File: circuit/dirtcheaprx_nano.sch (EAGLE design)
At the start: 20 parts, among them IC1 MCP1700

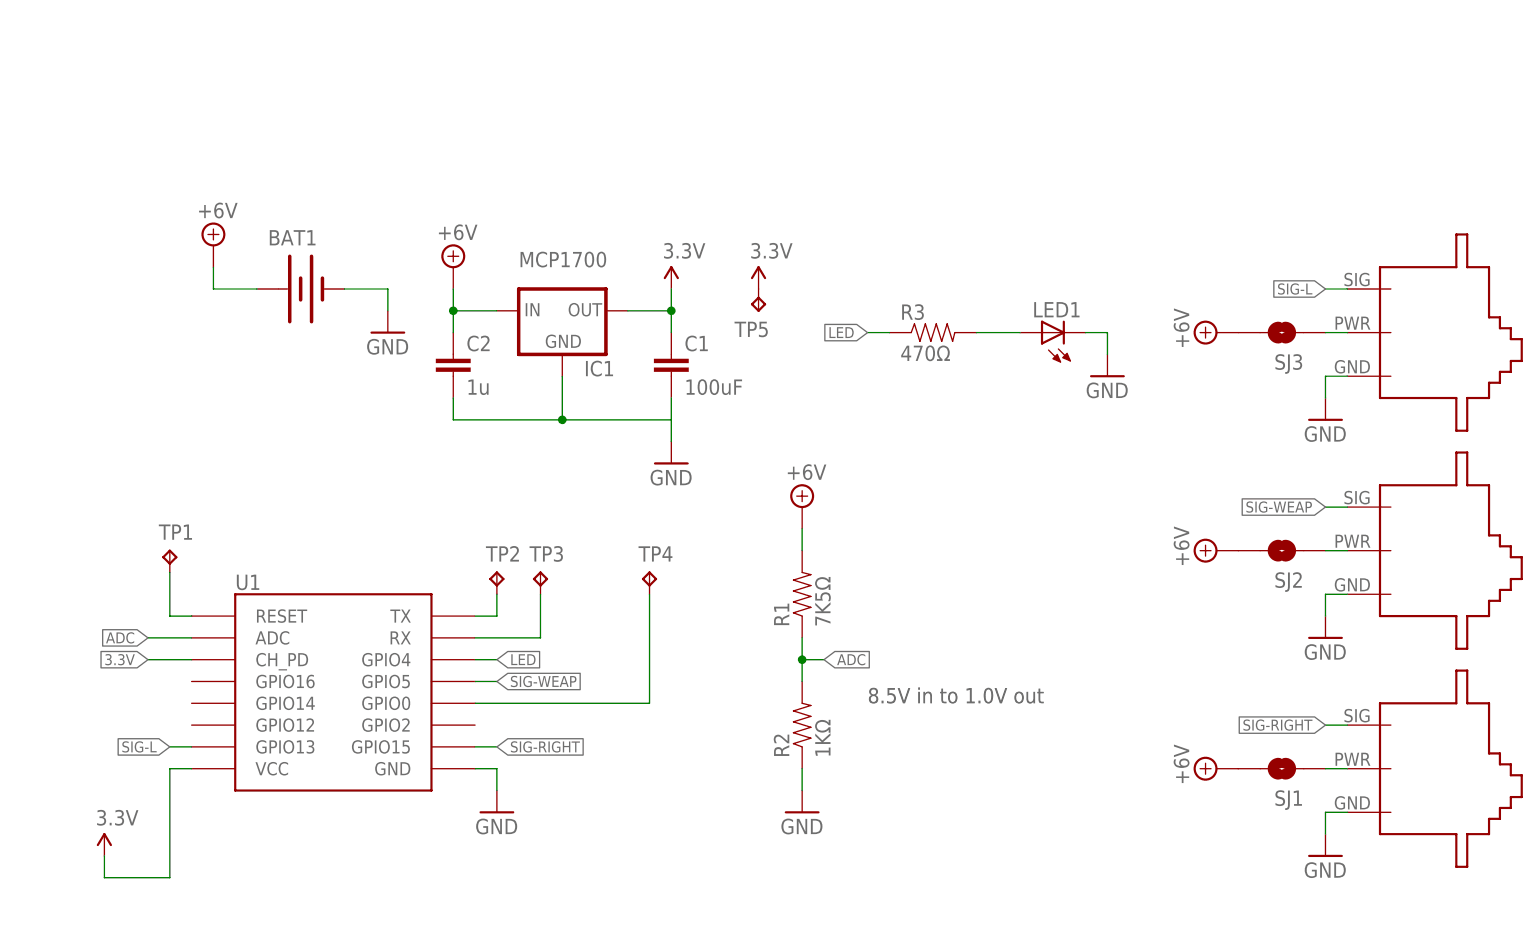
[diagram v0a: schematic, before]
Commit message: nano PCB for dirt cheap rx
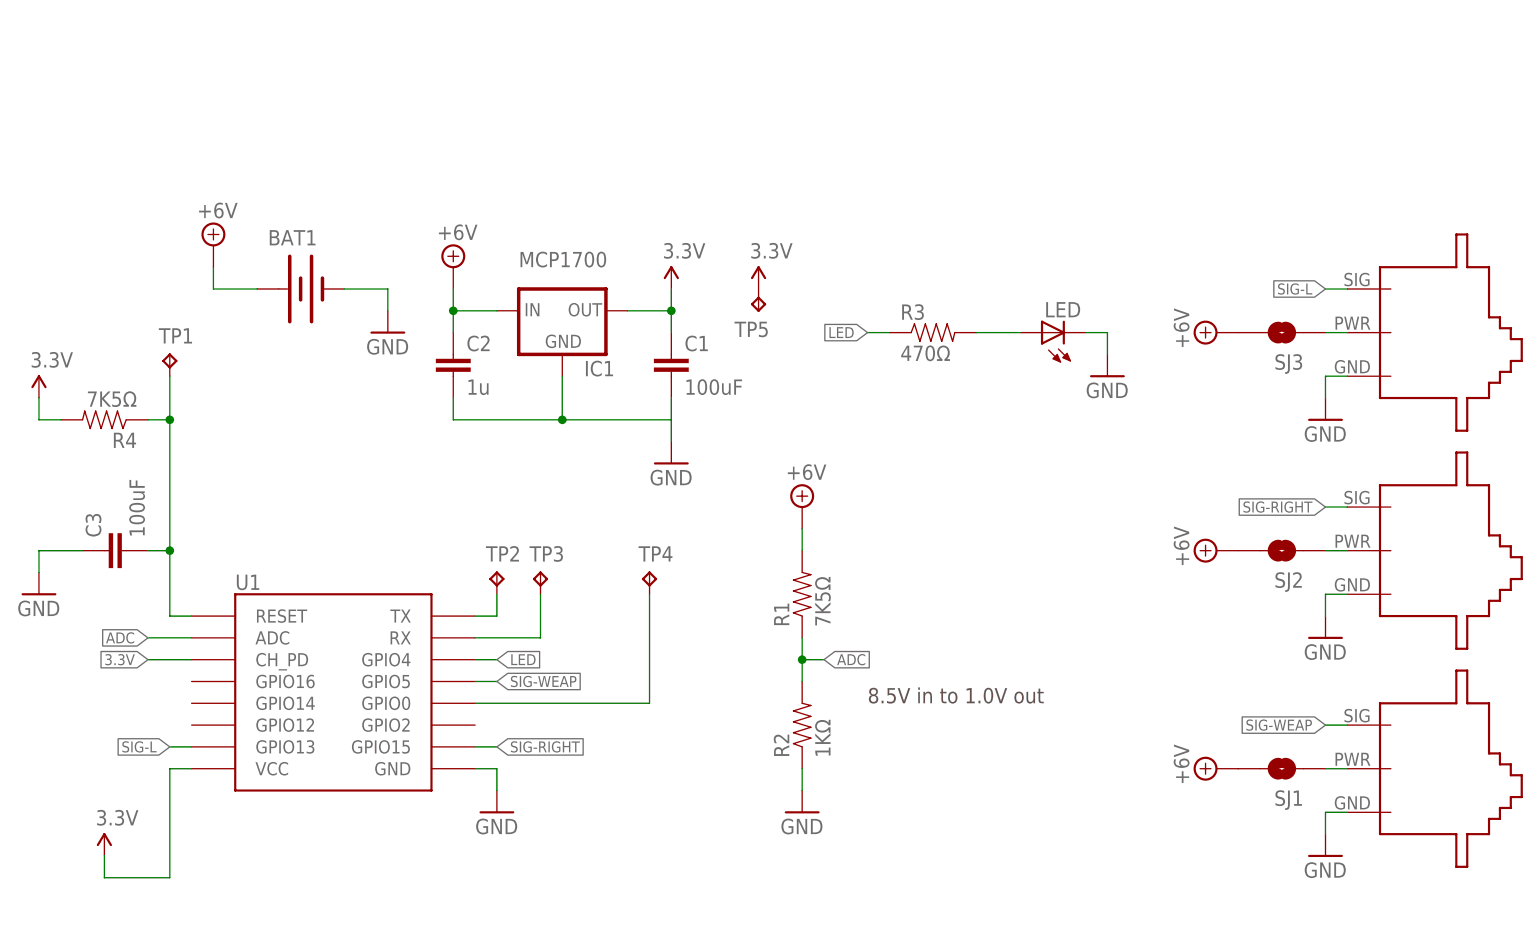
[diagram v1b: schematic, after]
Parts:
- removed LED1: (no value), dirtcheaprx:LED5MM
- added C3: 100uF, dirtcheaprx_nano:CAP0603-CAP
- added LED: (no value), dirtcheaprx_nano:LED5MM
- added R4: 7K5Ω, dirtcheaprx_nano:RESISTOR0603-RES
- BAT1: device dirtcheaprx:BATTERY-WIRE-CONN -> dirtcheaprx_nano:BATTERY-WIRE-CONN
- C1, C2: device dirtcheaprx:CAP0603-CAP -> dirtcheaprx_nano:CAP0603-CAP
- IC1: device dirtcheaprx:V_REG_78XX-SOT -> dirtcheaprx_nano:V_REG_78XX-SOT
- R1, R2, R3: device dirtcheaprx:RESISTOR0603-RES -> dirtcheaprx_nano:RESISTOR0603-RES
- SERVO1, SERVO2, SERVO3: value SERVO-1 -> SERVO-SMD-EDGE-1; device dirtcheaprx:SERVO-1 -> dirtcheaprx_nano:SERVO-SMD-EDGE-1
- SJ1, SJ2, SJ3: device dirtcheaprx:SOLDERJUMPERNO -> dirtcheaprx_nano:SOLDERJUMPERNO
- TP1, TP2, TP3, TP4, TP5: device dirtcheaprx:TPPAD1-13 -> dirtcheaprx_nano:TPPAD1-13
- U1: device dirtcheaprx:ESP12SMD -> dirtcheaprx_nano:ESP12SMD
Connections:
- net 3.3V: now also R4.2
- net GND: now also C3.1, LED.C; no longer LED1.C
- net N$1: now also LED.A; no longer LED1.A
- net N$8: now also C3.2, R4.1
- net SIG-RIGHT: now also SERVO2.SIG; no longer SERVO1.SIG
- net SIG-WEAP: now also SERVO1.SIG; no longer SERVO2.SIG
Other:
- moved on the sheet: TP1

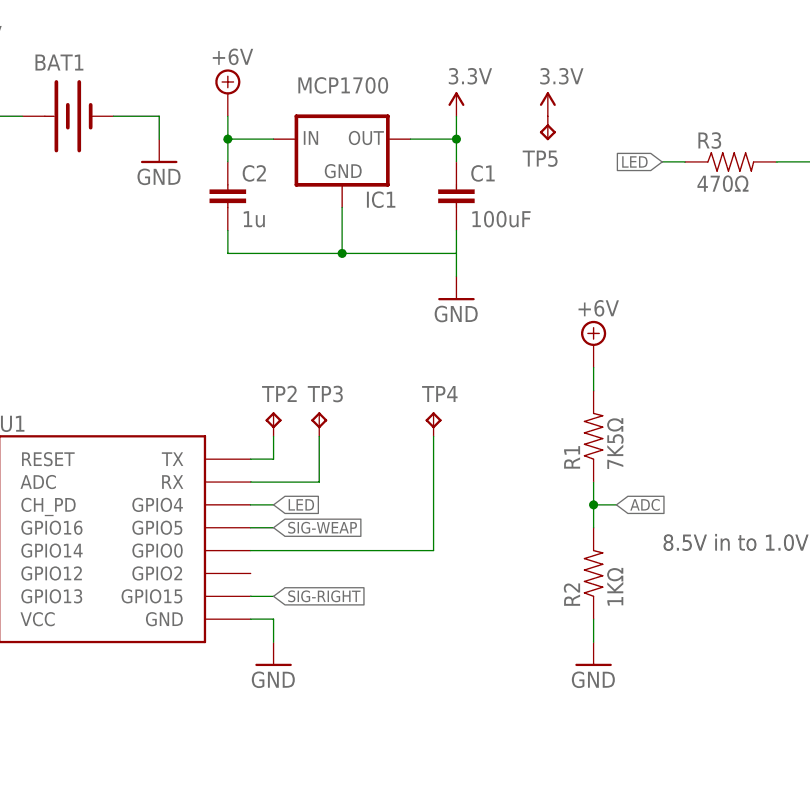
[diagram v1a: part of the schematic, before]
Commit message: GPIO15 needs to be pulled down, I missed the memo...
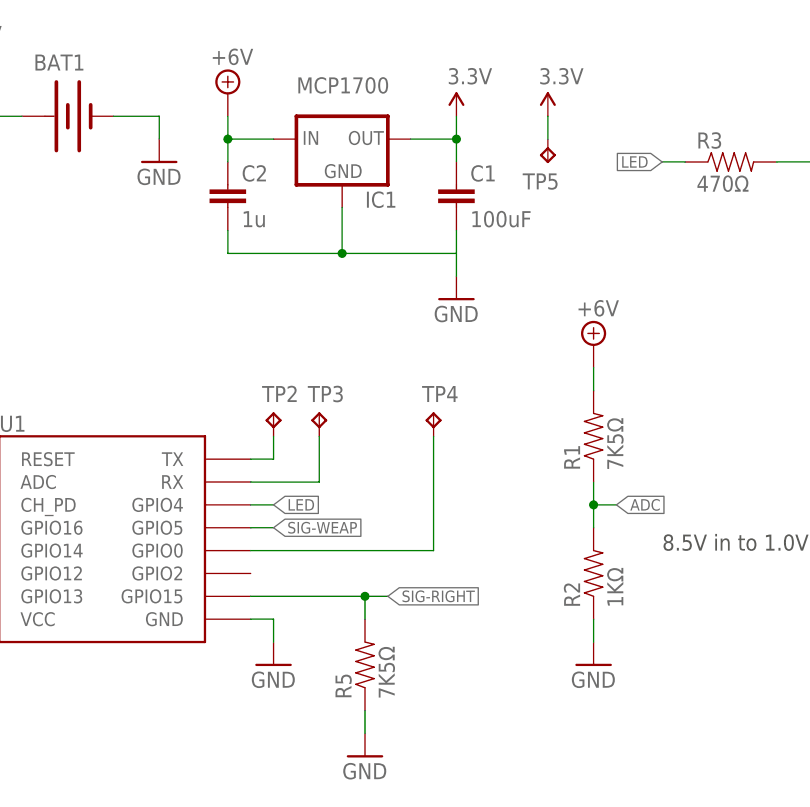
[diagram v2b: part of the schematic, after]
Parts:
- added R5: 7K5Ω, dirtcheaprx_nano:RESISTOR0603-RES
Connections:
- net GND: now also R5.1
- net SIG-RIGHT: now also R5.2
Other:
- moved on the sheet: TP5
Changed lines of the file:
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@@
 <grid distance="0.1" unitdist="inch" unit="inch" style="lines" multiple="1" display="no" altdistance="0.01" altunitdist="inch" altunit="inch"/>
 <layers>
-<layer number="1" name="Top" color="4" fill="1" visible="yes" active="no"/>
-<layer number="2" name="Route2" color="1" fill="3" visible="yes" active="no"/>
-<layer number="3" name="Route3" color="4" fill="3" visible="yes" active="no"/>
-<layer number="4" name="Route4" color="1" fill="4" visible="yes" active="no"/>
-<layer number="5" name="Route5" color="4" fill="4" visible="yes" active="no"/>
-<layer number="6" name="Route6" color="1" fill="8" visible="yes" active="no"/>
-<layer number="7" name="Route7" color="4" fill="8" visible="yes" active="no"/>
-<layer number="8" name="Route8" color="1" fill="2" visible="yes" active="no"/>
-<layer number="9" name="Route9" color="4" fill="2" visible="yes" active="no"/>
-<layer number="10" name="Route10" color="1" fill="7" visible="yes" active="no"/>
-<layer number="11" name="Route11" color="4" fill="7" visible="yes" active="no"/>
-<layer number="12" name="Route12" color="1" fill="5" visible="yes" active="no"/>
-<layer number="13" name="Route13" color="4" fill="5" visible="yes" active="no"/>
-<layer number="14" name="Route14" color="1" fill="6" visible="yes" active="no"/>
-<layer number="15" name="Route15" color="4" fill="6" visible="yes" active="no"/>
-<layer number="16" name="Bottom" color="1" fill="1" visible="yes" active="no"/>
-<layer number="17" name="Pads" color="2" fill="1" visible="yes" active="no"/>
-<layer number="18" name="Vias" color="2" fill="1" visible="yes" active="no"/>
-<layer number="19" name="Unrouted" color="6" fill="1" visible="yes" active="no"/>
-<layer number="20" name="Dimension" color="15" fill="1" visible="yes" active="no"/>
-<layer number="21" name="tPlace" color="7" fill="1" visible="yes" active="no"/>
-<layer number="22" name="bPlace" color="7" fill="1" visible="yes" active="no"/>
-<layer number="23" name="tOrigins" color="15" fill="1" visible="yes" active="no"/>
-<layer number="24" name="bOrigins" color="15" fill="1" visible="yes" active="no"/>
-<layer number="25" name="tNames" color="7" fill="1" visible="yes" active="no"/>
-<layer number="26" name="bNames" color="7" fill="1" visible="yes" active="no"/>
-<layer number="27" name="tValues" color="7" fill="1" visible="yes" active="no"/>
-<layer number="28" name="bValues" color="7" fill="1" visible="yes" active="no"/>
+<layer number="1" name="Top" color="4" fill="1" visible="no" active="no"/>
+<layer number="2" name="Route2" color="1" fill="3" visible="no" active="no"/>
+<layer number="3" name="Route3" color="4" fill="3" visible="no" active="no"/>
+<layer number="4" name="Route4" color="1" fill="4" visible="no" active="no"/>
+<layer number="5" name="Route5" color="4" fill="4" visible="no" active="no"/>
+<layer number="6" name="Route6" color="1" fill="8" visible="no" active="no"/>
+<layer number="7" name="Route7" color="4" fill="8" visible="no" active="no"/>
+<layer number="8" name="Route8" color="1" fill="2" visible="no" active="no"/>
+<layer number="9" name="Route9" color="4" fill="2" visible="no" active="no"/>
+<layer number="10" name="Route10" color="1" fill="7" visible="no" active="no"/>
+<layer number="11" name="Route11" color="4" fill="7" visible="no" active="no"/>
+<layer number="12" name="Route12" color="1" fill="5" visible="no" active="no"/>
+<layer number="13" name="Route13" color="4" fill="5" visible="no" active="no"/>
+<layer number="14" name="Route14" color="1" fill="6" visible="no" active="no"/>
+<layer number="15" name="Route15" color="4" fill="6" visible="no" active="no"/>
+<layer number="16" name="Bottom" color="1" fill="1" visible="no" active="no"/>
+<layer number="17" name="Pads" color="2" fill="1" visible="no" active="no"/>
+<layer number="18" name="Vias" color="2" fill="1" visible="no" active="no"/>
+<layer number="19" name="Unrouted" color="6" fill="1" visible="no" active="no"/>
+<layer number="20" name="Dimension" color="15" fill="1" visible="no" active="no"/>
+<layer number="21" name="tPlace" color="7" fill="1" visible="no" active="no"/>
+<layer number="22" name="bPlace" color="7" fill="1" visible="no" active="no"/>
+<layer number="23" name="tOrigins" color="15" fill="1" visible="no" active="no"/>
+<layer number="24" name="bOrigins" color="15" fill="1" visible="no" active="no"/>
+<layer number="25" name="tNames" color="7" fill="1" visible="no" active="no"/>
+<layer number="26" name="bNames" color="7" fill="1" visible="no" active="no"/>
+<layer number="27" name="tValues" color="7" fill="1" visible="no" active="no"/>
+<layer number="28" name="bValues" color="7" fill="1" visible="no" active="no"/>
 <layer number="29" name="tStop" color="7" fill="3" visible="no" active="no"/>
 <layer number="30" name="bStop" color="7" fill="6" visible="no" active="no"/>
@@
 <layer number="35" name="tGlue" color="7" fill="4" visible="no" active="no"/>
 <layer number="36" name="bGlue" color="7" fill="5" visible="no" active="no"/>
-<layer number="37" name="tTest" color="7" fill="1" visible="yes" active="no"/>
-<layer number="38" name="bTest" color="7" fill="1" visible="yes" active="no"/>
+<layer number="37" name="tTest" color="7" fill="1" visible="no" active="no"/>
+<layer number="38" name="bTest" color="7" fill="1" visible="no" active="no"/>
 <layer number="39" name="tKeepout" color="4" fill="11" visible="no" active="no"/>
 <layer number="40" name="bKeepout" color="1" fill="11" visible="no" active="no"/>
@@
 <layer number="44" name="Drills" color="7" fill="1" visible="no" active="no"/>
 <layer number="45" name="Holes" color="7" fill="1" visible="no" active="no"/>
-<layer number="46" name="Milling" color="3" fill="1" visible="yes" active="no"/>
-<layer number="47" name="Measures" color="7" fill="1" visible="yes" active="no"/>
-<layer number="48" name="Document" color="7" fill="1" visible="yes" active="no"/>
-<layer number="49" name="Reference" color="7" fill="1" visible="yes" active="no"/>
-<layer number="50" name="dxf" color="7" fill="1" visible="yes" active="no"/>
-<layer number="51" name="tDocu" color="7" fill="1" visible="yes" active="no"/>
-<layer number="52" name="bDocu" color="7" fill="1" visible="yes" active="no"/>
-<layer number="53" name="tGND_GNDA" color="7" fill="9" visible="yes" active="no"/>
-<layer number="54" name="bGND_GNDA" color="1" fill="9" visible="yes" active="no"/>
-<layer number="56" name="wert" color="7" fill="1" visible="yes" active="no"/>
+<layer number="46" name="Milling" color="3" fill="1" visible="no" active="no"/>
+<layer number="47" name="Measures" color="7" fill="1" visible="no" active="no"/>
+<layer number="48" name="Document" color="7" fill="1" visible="no" active="no"/>
+<layer number="49" name="Reference" color="7" fill="1" visible="no" active="no"/>
+<layer number="50" name="dxf" color="7" fill="1" visible="no" active="no"/>
+<layer number="51" name="tDocu" color="7" fill="1" visible="no" active="no"/>
+<layer number="52" name="bDocu" color="7" fill="1" visible="no" active="no"/>
+<layer number="53" name="tGND_GNDA" color="7" fill="9" visible="no" active="no"/>
+<layer number="54" name="bGND_GNDA" color="1" fill="9" visible="no" active="no"/>
+<layer number="56" name="wert" color="7" fill="1" visible="no" active="no"/>
 <layer number="88" name="SimResults" color="9" fill="1" visible="no" active="yes"/>
 <layer number="89" name="SimProbes" color="9" fill="1" visible="no" active="yes"/>
@@
 <part name="P+4" library="dirtcheaprx_nano" deviceset="3.3V" device=""/>
 <part name="GND9" library="dirtcheaprx_nano" deviceset="GND" device=""/>
+<part name="R5" library="dirtcheaprx_nano" deviceset="RESISTOR" device="0603-RES" value="7K5Ω"/>
+<part name="GND10" library="dirtcheaprx_nano" deviceset="GND" device=""/>
 </parts>
 <sheets>
@@
 <instance part="TP4" gate="G$1" x="40.64" y="2.54"/>
 <instance part="GND8" gate="1" x="93.98" y="25.4"/>
-<instance part="TP5" gate="G$1" x="53.34" y="33.02" rot="R180"/>
+<instance part="TP5" gate="G$1" x="53.34" y="30.48" rot="R180"/>
 <instance part="P+3" gate="G$1" x="53.34" y="35.56"/>
 <instance part="SUPPLY4" gate="G$1" x="106.68" y="-20.32" rot="R90"/>
@@
 <instance part="P+4" gate="G$1" x="-30.48" y="22.86"/>
 <instance part="GND9" gate="1" x="-30.48" y="0"/>
+<instance part="R5" gate="G$1" x="33.02" y="-25.4" rot="R90"/>
+<instance part="GND10" gate="1" x="33.02" y="-35.56"/>
 </instances>
 <busses>
@@
 <pinref part="TP5" gate="G$1" pin="TP"/>
 <pinref part="P+3" gate="G$1" pin="3.3V"/>
+<wire x1="53.34" y1="33.02" x2="53.34" y2="35.56" width="0.1524" layer="91"/>
 </segment>
 <segment>
@@
 <wire x1="-30.48" y1="5.08" x2="-30.48" y2="2.54" width="0.1524" layer="91"/>
 </segment>
+<segment>
+<pinref part="GND10" gate="1" pin="GND"/>
+<pinref part="R5" gate="G$1" pin="1"/>
+<wire x1="33.02" y1="-33.02" x2="33.02" y2="-30.48" width="0.1524" layer="91"/>
+</segment>
 </net>
 <net name="ADC" class="0">
@@
 <segment>
 <pinref part="U1" gate="G$1" pin="GPIO15"/>
-<wire x1="20.32" y1="-17.78" x2="22.86" y2="-17.78" width="0.1524" layer="91"/>
-<label x="22.86" y="-17.78" size="1.27" layer="95" xref="yes"/>
-</segment>
-<segment>
+<wire x1="20.32" y1="-17.78" x2="33.02" y2="-17.78" width="0.1524" layer="91"/>
+<label x="35.56" y="-17.78" size="1.27" layer="95" xref="yes"/>
+<pinref part="R5" gate="G$1" pin="2"/>
+<wire x1="33.02" y1="-17.78" x2="35.56" y2="-17.78" width="0.1524" layer="91"/>
+<wire x1="33.02" y1="-20.32" x2="33.02" y2="-17.78" width="0.1524" layer="91"/>
+<junction x="33.02" y="-17.78"/>
+</segment>
+<segment>

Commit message: corrected GPIO4 and GPIO5 mixup in PCBs
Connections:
- net LED: now also U1.GPIO5; no longer U1.GPIO4
- net SIG-WEAP: now also U1.GPIO4; no longer U1.GPIO5
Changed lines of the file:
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@@
 <net name="LED" class="0">
 <segment>
-<pinref part="U1" gate="G$1" pin="GPIO4"/>
+<pinref part="U1" gate="G$1" pin="GPIO5"/>
 <wire x1="20.32" y1="-7.62" x2="22.86" y2="-7.62" width="0.1524" layer="91"/>
 <label x="22.86" y="-7.62" size="1.27" layer="95" xref="yes"/>
@@
 <net name="SIG-WEAP" class="0">
 <segment>
-<pinref part="U1" gate="G$1" pin="GPIO5"/>
+<pinref part="U1" gate="G$1" pin="GPIO4"/>
 <wire x1="20.32" y1="-10.16" x2="22.86" y2="-10.16" width="0.1524" layer="91"/>
 <label x="22.86" y="-10.16" size="1.27" layer="95" xref="yes"/>

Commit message: better battery reading
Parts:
- C1: value 100uF -> 4u7; device dirtcheaprx_nano:CAP0603-CAP -> dirtcheaprx_nano:CAP0805
- C2: value 1u -> 22u; device dirtcheaprx_nano:CAP0603-CAP -> dirtcheaprx_nano:CAP0805
- C3: value 100uF -> 100n
- IC1: value MCP1700 -> MCP1703T-3302E/CB
- R1, R4, R5: value 7K5Ω -> 5K6Ω
- R2: value 1KΩ -> 470Ω
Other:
- note added: "12.9V in to 1.0V out"
- note removed: "8.5V in to 1.0V out"
